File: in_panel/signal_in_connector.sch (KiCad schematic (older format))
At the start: 5 parts, among them J601 Sensor

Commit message: More work on in_panel.  Also, shortened input_board by 10mm and tweaked the testpoints a bit, added another GND, and changed the supply TPs to be a hookable type.
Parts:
- J601: footprint Connector_RJ:RJ45_Amphenol_RJHSE538X -> input:RJ45_Amphenol_RJHSE5380; DK line 18 -> (none); Description CONN MOD JACK 8P8C R/A SHIELDED -> (none); Digikey RJHSE5387-ND -> (none); MPN RJHSE5387 -> (none)
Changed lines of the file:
@@
 AR Path="/60030EBA/6001FBAB/5E75AFBD" Ref="J1101"  Part="1"
 AR Path="/60030EFF/6001FBAB/5E75AFBD" Ref="J1601"  Part="1"
-F 0 "J1601" H 3950 3450 50  0000 R CNN
+F 0 "J601" H 3950 3450 50  0000 R CNN
 F 1 "Sensor" H 4050 3450 50  0000 L CNN
-F 2 "Connector_RJ:RJ45_Amphenol_RJHSE538X" V 4150 2925 50  0001 C CNN
-F 3 "https://cdn.amphenol-icc.com/media/wysiwyg/files/drawing/rjhse538x.pdf" V 4150 2925 50  0001 C CNN
-F 4 "RJHSE5387-ND" H 4150 2900 50  0001 C CNN "Digikey"
-F 5 "RJHSE5387" H 4150 2900 50  0001 C CNN "MPN"
-F 6 "CONN MOD JACK 8P8C R/A SHIELDED" H 4150 2900 50  0001 C CNN "Description"
-F 7 "18" H 4150 2900 50  0001 C CNN "DK line"
+F 2 "input:RJ45_Amphenol_RJHSE5380" V 4150 2925 50  0001 C CNN
+F 3 "" V 4150 2925 50  0001 C CNN
+F 4 "" H 4150 2900 50  0001 C CNN "Digikey"
+F 5 "" H 4150 2900 50  0001 C CNN "MPN"
+F 6 "" H 4150 2900 50  0001 C CNN "Description"
+F 7 "" H 4150 2900 50  0001 C CNN "DK line"
 F 8 "Amphenol ICC (Commercial Products)" H 4150 2900 50  0001 C CNN "Manufacturer"
 	1    4150 2900
@@
 AR Path="/60030EBA/6001FBAB/5E75F20B" Ref="FB1101"  Part="1"
 AR Path="/60030EFF/6001FBAB/5E75F20B" Ref="FB1601"  Part="1"
-F 0 "FB1601" H 5500 4487 60  0000 C CNN
+F 0 "FB601" H 5500 4487 60  0000 C CNN
 F 1 "2K Ohm" H 5500 4381 60  0000 C CNN
 F 2 "Inductor_SMD:L_0805_2012Metric" H 5700 4400 60  0001 L CNN
@@
 AR Path="/60030EBA/6001FBAB/5E7695B8" Ref="D1101"  Part="1"
 AR Path="/60030EFF/6001FBAB/5E7695B8" Ref="D1601"  Part="1"
-F 0 "D1601" H 6000 4650 50  0000 C CNN
+F 0 "D601" H 6000 4650 50  0000 C CNN
 F 1 "5V (standoff)" H 6100 4350 50  0000 C CNN
 F 2 "Diode_SMD:D_SMA" H 6000 4550 50  0001 C CNN
@@
 AR Path="/60030EBA/6001FBAB/5E76B461" Ref="FB1102"  Part="1"
 AR Path="/60030EFF/6001FBAB/5E76B461" Ref="FB1602"  Part="1"
-F 0 "FB1602" H 6500 4487 60  0000 C CNN
+F 0 "FB602" H 6500 4487 60  0000 C CNN
 F 1 "2K Ohm" H 6500 4381 60  0000 C CNN
 F 2 "Inductor_SMD:L_0805_2012Metric" H 6700 4400 60  0001 L CNN
@@
 AR Path="/60030EBA/6001FBAB/5E76E2C4" Ref="C1101"  Part="1"
 AR Path="/60030EFF/6001FBAB/5E76E2C4" Ref="C1601"  Part="1"
-F 0 "C1601" H 4992 4546 50  0000 L CNN
+F 0 "C601" H 4992 4546 50  0000 L CNN
 F 1 "1nF" H 4992 4455 50  0000 L CNN
 F 2 "Capacitor_SMD:C_0805_2012Metric" H 4900 4500 50  0001 C CNN
@@
 AR Path="/60030EBA/6001FBAB/5E36FAA0" Ref="#PWR01101"  Part="1"
 AR Path="/60030EFF/6001FBAB/5E36FAA0" Ref="#PWR01601"  Part="1"
-F 0 "#PWR01601" H 4150 3300 50  0001 C CNN
+F 0 "#PWR0601" H 4150 3300 50  0001 C CNN
 F 1 "Earth" H 4150 3400 50  0001 C CNN
 F 2 "" H 4150 3550 50  0001 C CNN
@@
 AR Path="/60030EBA/6001FBAB/5E36FFC7" Ref="#PWR01102"  Part="1"
 AR Path="/60030EFF/6001FBAB/5E36FFC7" Ref="#PWR01602"  Part="1"
-F 0 "#PWR01602" H 4900 4550 50  0001 C CNN
+F 0 "#PWR0602" H 4900 4550 50  0001 C CNN
 F 1 "Earth" H 4900 4650 50  0001 C CNN
 F 2 "" H 4900 4800 50  0001 C CNN
@@
 AR Path="/60030EBA/6001FBAB/5E370459" Ref="#PWR01103"  Part="1"
 AR Path="/60030EFF/6001FBAB/5E370459" Ref="#PWR01603"  Part="1"
-F 0 "#PWR01603" H 6000 4550 50  0001 C CNN
+F 0 "#PWR0603" H 6000 4550 50  0001 C CNN
 F 1 "Earth" H 6000 4650 50  0001 C CNN
 F 2 "" H 6000 4800 50  0001 C CNN

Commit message: in_panel is nearly complete, input/adc.sch: change testpoint style to loop. input/input_channel.sch: modification seems spurious
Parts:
- added J602: Sensor, input:HR10_connector, symbol Connector_Generic:Conn_01x10
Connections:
- net labels added: config1, config2
- wire segments 21 -> 30
- no-connect marks 0 -> 2
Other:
- moved on the sheet: C1601, D1601, FB1601, FB1602, J1601

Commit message: Revision 0 of in_panel, off to fab
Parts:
- C601: DK line 1 -> I.1
- D601: DK line 40 -> I.40
- FB601, FB602: DK line 5 -> I.5
- J601: footprint input:RJ45_Amphenol_RJHSE5380 -> input:RJ45_Amphenol_RJHSE-338x; DK line (none) -> IP.5; Description (none) -> CONN MOD JACK 8P8C VERT SHIELDED; Digikey (none) -> RJHSE-3380-ND; MPN (none) -> RJHSE-3380
- J602: DK line (none) -> IP.1; Description (none) -> CONN RCPT MALE 12POS SILV SOLDER; Digikey (none) -> H124032-ND; MPN (none) -> HR10G-10R-12PB(71); Manufacturer (none) -> Hirose Electric Co Ltd
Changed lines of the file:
@@
 AR Path="/60030EBA/6001FBAB/5E75AFBD" Ref="J1101"  Part="1"
 AR Path="/60030EFF/6001FBAB/5E75AFBD" Ref="J1601"  Part="1"
-F 0 "J1601" H 3100 4650 50  0000 R CNN
+F 0 "J601" H 3100 4650 50  0000 R CNN
 F 1 "Sensor" H 3200 4650 50  0000 L CNN
-F 2 "input:RJ45_Amphenol_RJHSE5380" V 3300 4125 50  0001 C CNN
-F 3 "" V 3300 4125 50  0001 C CNN
-F 4 "" H 3300 4100 50  0001 C CNN "Digikey"
-F 5 "" H 3300 4100 50  0001 C CNN "MPN"
-F 6 "" H 3300 4100 50  0001 C CNN "Description"
-F 7 "" H 3300 4100 50  0001 C CNN "DK line"
+F 2 "input:RJ45_Amphenol_RJHSE-338x" V 3300 4125 50  0001 C CNN
+F 3 "http://www.amphenol-icc.com/media/wysiwyg/files/drawing/rjhse338x.pdf" V 3300 4125 50  0001 C CNN
+F 4 "RJHSE-3380-ND" H 3300 4100 50  0001 C CNN "Digikey"
+F 5 "RJHSE-3380" H 3300 4100 50  0001 C CNN "MPN"
+F 6 "CONN MOD JACK 8P8C VERT SHIELDED" H 3300 4100 50  0001 C CNN "Description"
+F 7 "IP.5" H 3300 4100 50  0001 C CNN "DK line"
 F 8 "Amphenol ICC (Commercial Products)" H 3300 4100 50  0001 C CNN "Manufacturer"
 	1    3300 4100
@@
 AR Path="/60030EBA/6001FBAB/5E75F20B" Ref="FB1101"  Part="1"
 AR Path="/60030EFF/6001FBAB/5E75F20B" Ref="FB1601"  Part="1"
-F 0 "FB1601" H 4650 5687 60  0000 C CNN
+F 0 "FB601" H 4650 5687 60  0000 C CNN
 F 1 "2K Ohm" H 4650 5581 60  0000 C CNN
 F 2 "Inductor_SMD:L_0805_2012Metric" H 4850 5600 60  0001 L CNN
@@
 F 11 "Laird-Signal Integrity Products" H 4850 6500 60  0001 L CNN "Manufacturer"
 F 12 "Active" H 4850 6600 60  0001 L CNN "Status"
-F 13 "5" H 4650 5400 50  0001 C CNN "DK line"
+F 13 "I.5" H 4650 5400 50  0001 C CNN "DK line"
 F 14 "240-2396-1-ND" H 4650 5400 50  0001 C CNN "Digikey"
 	1    4650 5400
@@
 AR Path="/60030EBA/6001FBAB/5E7695B8" Ref="D1101"  Part="1"
 AR Path="/60030EFF/6001FBAB/5E7695B8" Ref="D1601"  Part="1"
-F 0 "D1601" H 5150 5850 50  0000 C CNN
+F 0 "D601" H 5150 5850 50  0000 C CNN
 F 1 "5V (standoff)" H 5250 5550 50  0000 C CNN
 F 2 "Diode_SMD:D_SMA" H 5150 5750 50  0001 C CNN
@@
 F 5 "TVS DIODE 5V 9.2V DO214AC" H 5150 5750 50  0001 C CNN "Description"
 F 6 "732-9974-1-ND" H 5150 5750 50  0001 C CNN "Digikey"
-F 7 "40" H 5150 5750 50  0001 C CNN "DK line"
+F 7 "I.40" H 5150 5750 50  0001 C CNN "DK line"
 F 8 "Würth Elektronik" H 5150 5750 50  0001 C CNN "Manufacturer"
 	1    5150 5750
@@
 AR Path="/60030EBA/6001FBAB/5E76B461" Ref="FB1102"  Part="1"
 AR Path="/60030EFF/6001FBAB/5E76B461" Ref="FB1602"  Part="1"
-F 0 "FB1602" H 5650 5687 60  0000 C CNN
+F 0 "FB602" H 5650 5687 60  0000 C CNN
 F 1 "2K Ohm" H 5650 5581 60  0000 C CNN
 F 2 "Inductor_SMD:L_0805_2012Metric" H 5850 5600 60  0001 L CNN
@@
 F 11 "Laird-Signal Integrity Products" H 5850 6500 60  0001 L CNN "Manufacturer"
 F 12 "Active" H 5850 6600 60  0001 L CNN "Status"
-F 13 "5" H 5650 5400 50  0001 C CNN "DK line"
+F 13 "I.5" H 5650 5400 50  0001 C CNN "DK line"
 F 14 "240-2396-1-ND" H 5650 5400 50  0001 C CNN "Digikey"
 	1    5650 5400
@@
 AR Path="/60030EBA/6001FBAB/5E76E2C4" Ref="C1101"  Part="1"
 AR Path="/60030EFF/6001FBAB/5E76E2C4" Ref="C1601"  Part="1"
-F 0 "C1601" H 4142 5746 50  0000 L CNN
+F 0 "C601" H 4142 5746 50  0000 L CNN
 F 1 "1nF" H 4142 5655 50  0000 L CNN
 F 2 "Capacitor_SMD:C_0805_2012Metric" H 4050 5700 50  0001 C CNN
@@
 F 5 "CC0805FRNPO0BN102" H 4050 5700 50  0001 C CNN "MPN"
 F 6 "CAP CER 1000PF 100V NPO 0805" H 4050 5700 50  0001 C CNN "Description"
-F 7 "1" H 4050 5700 50  0001 C CNN "DK line"
+F 7 "I.1" H 4050 5700 50  0001 C CNN "DK line"
 F 8 "Yageo" H 4050 5700 50  0001 C CNN "Manufacturer"
 	1    4050 5700
@@
 AR Path="/60030EBA/6001FBAB/600AD0FC" Ref="J1102"  Part="1"
 AR Path="/60030EFF/6001FBAB/600AD0FC" Ref="J1602"  Part="1"
-F 0 "J1602" H 3100 3000 50  0000 C CNN
+F 0 "J602" H 3100 3000 50  0000 C CNN
 F 1 "Sensor" H 3100 1900 50  0000 C CNN
 F 2 "input:HR10_connector" H 3100 2500 50  0001 C CNN
-F 3 "~" H 3100 2500 50  0001 C CNN
+F 3 "https://media.digikey.com/pdf/Data%20Sheets/Hirose%20PDFs/HR10.pdf" H 3100 2500 50  0001 C CNN
+F 4 "IP.1" H 3100 2500 50  0001 C CNN "DK line"
+F 5 "CONN RCPT MALE 12POS SILV SOLDER" H 3100 2500 50  0001 C CNN "Description"
+F 6 "H124032-ND" H 3100 2500 50  0001 C CNN "Digikey"
+F 7 "HR10G-10R-12PB(71)" H 3100 2500 50  0001 C CNN "MPN"
+F 8 "Hirose Electric Co Ltd" H 3100 2500 50  0001 C CNN "Manufacturer"
 	1    3100 2500
 	-1   0    0    -1

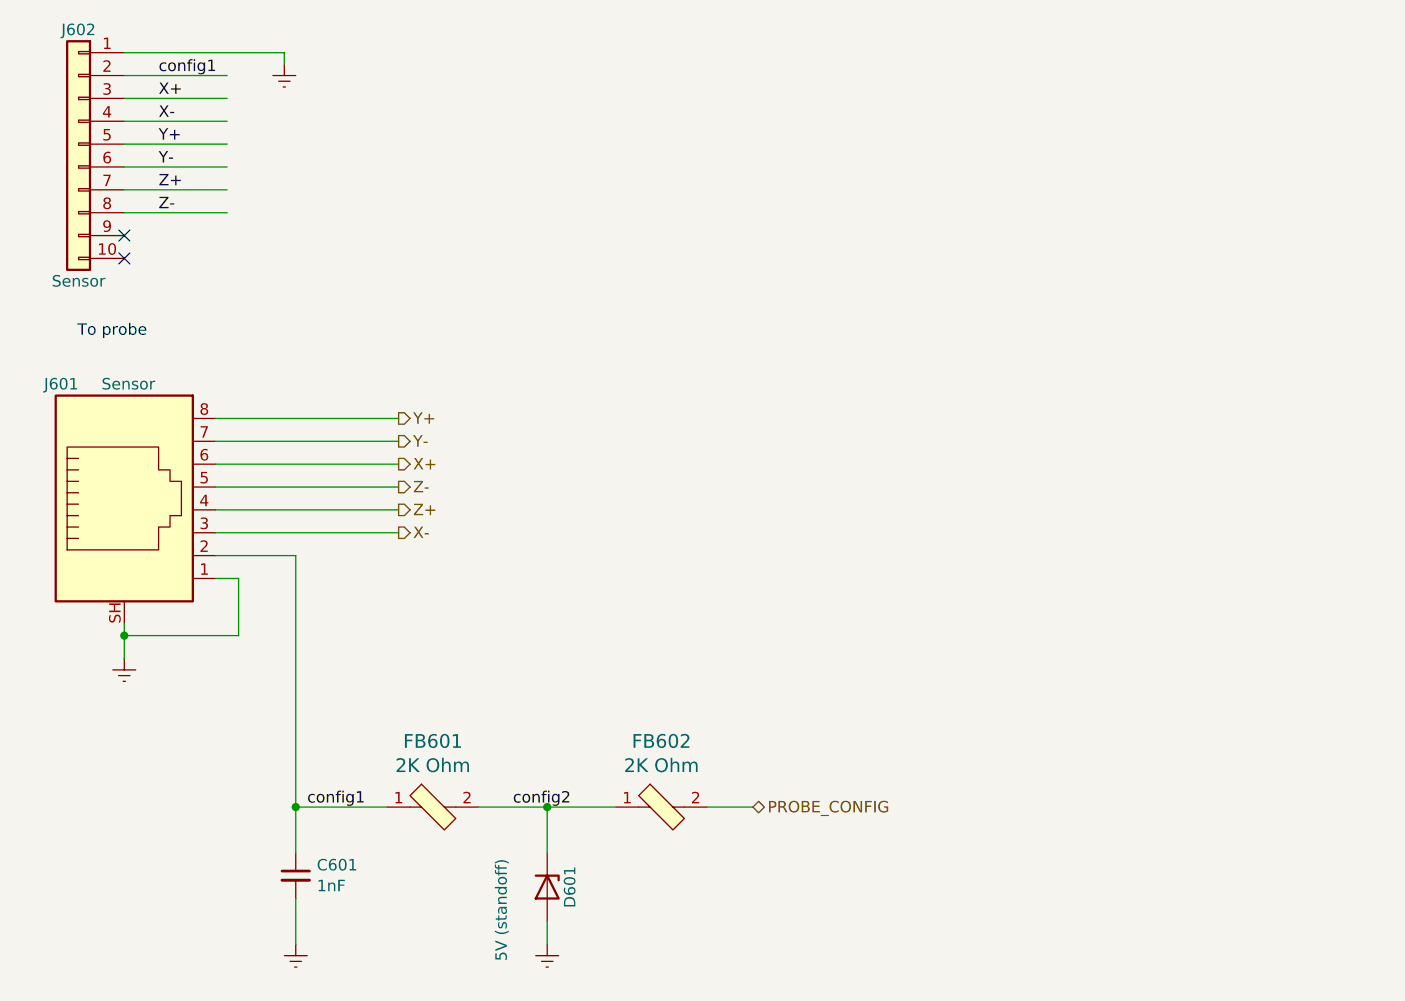
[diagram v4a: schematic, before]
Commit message: Mainly much more detailed documentation of the sensor pinout wrt the RJ45 standards, see docs/Rj45_probe_pinout.xlsx
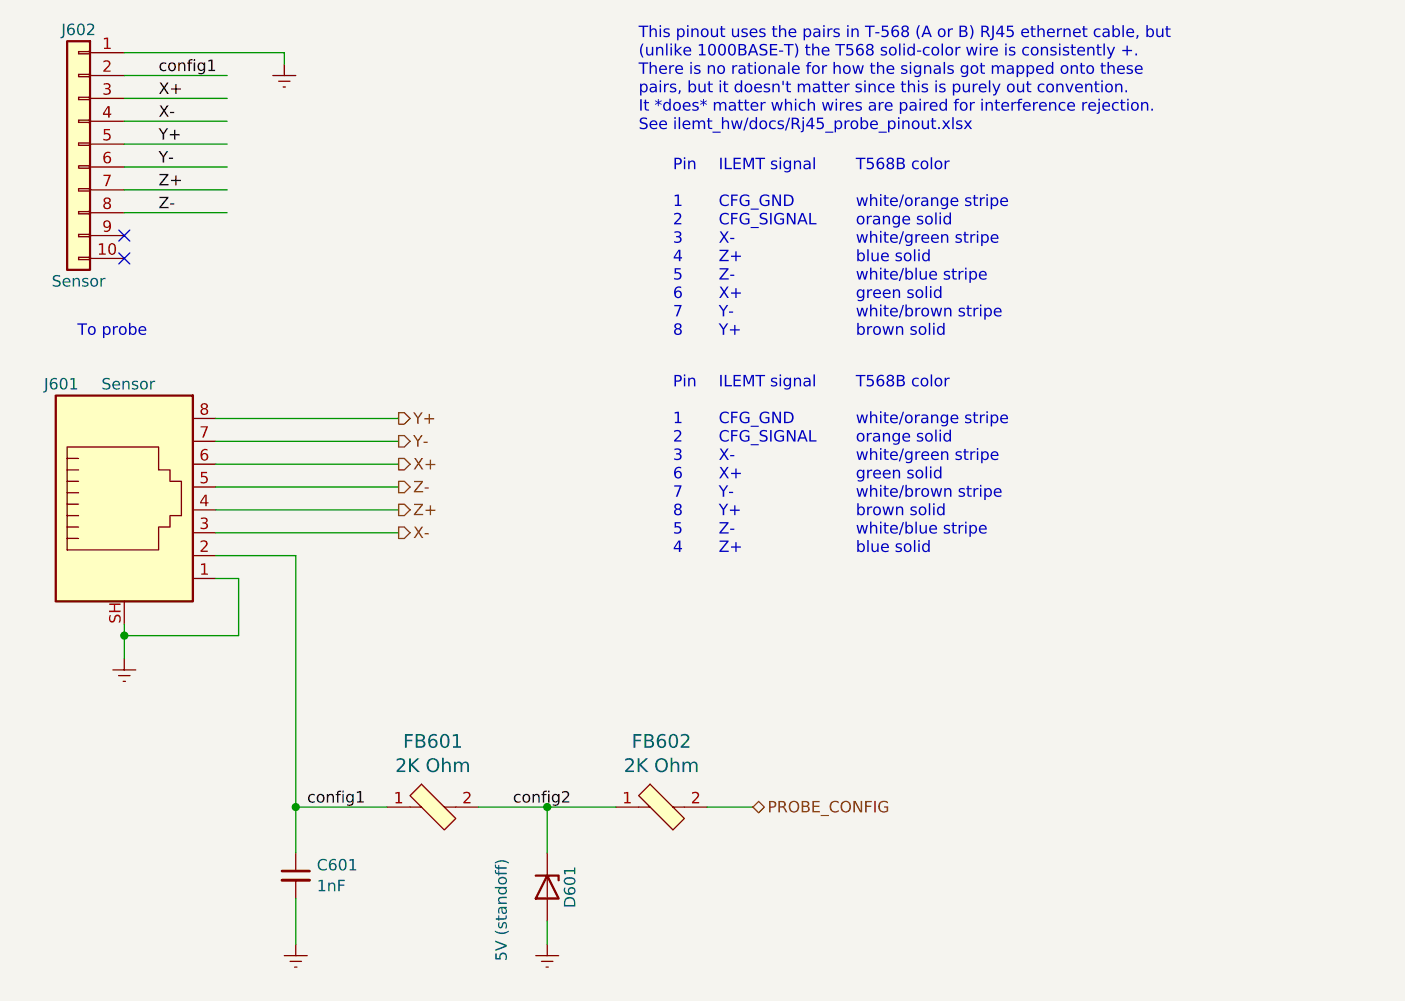
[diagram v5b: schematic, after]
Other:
- note added: "ILEMT signal\n\nCFG_GND\nCFG_SIGNAL\nX-\nX+\nY-\nY+\nZ-\nZ+\n"
- note added: "ILEMT signal\n\nCFG_GND\nCFG_SIGNAL\nX-\nZ+\nZ-\nX+\nY-\nY+\n"
- note added: "Pin\n\n1\n2\n3\n4\n5\n6\n7\n8\n"
- note added: "Pin\n\n1\n2\n3\n6\n7\n8\n5\n4"
- note added: "T568B color\n\nwhite/orange stripe\norange solid\nwhite/green stripe\nblue solid\nwhite/blue stripe\ngreen solid\nwhite/brown stripe\nbrown solid\n"
- note added: "T568B color\n\nwhite/orange stripe\norange solid\nwhite/green stripe\ngreen solid\nwhite/brown stripe\nbrown solid\nwhite/blue stripe\nblue solid"
- note added: "This pinout uses the pairs in T-568 (A or B) RJ45 ethernet cable, but\n(unlike 1000BASE-T) the T568 solid-color wire is consistently +.\nThere is no rationale for how the signals got mapped onto these\npairs, but it doesn't matter since this is purely out convention.\nIt *does* matter which wires are paired for interference rejection.\nSee ilemt_hw/docs/Rj45_probe_pinout.xlsx"
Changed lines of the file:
@@
 Wire Wire Line
 	3300 2100 4000 2100
+Text Notes 5550 2450 0    50   ~ 0
+This pinout uses the pairs in T-568 (A or B) RJ45 ethernet cable, but\n(unlike 1000BASE-T) the T568 solid-color wire is consistently +.\nThere is no rationale for how the signals got mapped onto these\npairs, but it doesn't matter since this is purely out convention.\nIt *does* matter which wires are paired for interference rejection.\nSee ilemt_hw/docs/Rj45_probe_pinout.xlsx
+Text Notes 5900 3350 0    50   ~ 0
+ILEMT signal\n\nCFG_GND\nCFG_SIGNAL\nX-\nZ+\nZ-\nX+\nY-\nY+\n
+Text Notes 5700 3350 0    50   ~ 0
+Pin\n\n1\n2\n3\n4\n5\n6\n7\n8\n
+Text Notes 6500 3350 0    50   ~ 0
+T568B color\n\nwhite/orange stripe\norange solid\nwhite/green stripe\nblue solid\nwhite/blue stripe\ngreen solid\nwhite/brown stripe\nbrown solid\n
+Text Notes 5900 4300 0    50   ~ 0
+ILEMT signal\n\nCFG_GND\nCFG_SIGNAL\nX-\nX+\nY-\nY+\nZ-\nZ+\n
+Text Notes 6500 4300 0    50   ~ 0
+T568B color\n\nwhite/orange stripe\norange solid\nwhite/green stripe\ngreen solid\nwhite/brown stripe\nbrown solid\nwhite/blue stripe\nblue solid
+Text Notes 5700 4300 0    50   ~ 0
+Pin\n\n1\n2\n3\n6\n7\n8\n5\n4
 $EndSCHEMATC
